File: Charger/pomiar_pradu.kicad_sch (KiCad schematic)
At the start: 13 parts, among them Q17 IRF7404, Q18 IRF7404, Q19 BC846, U10 MCP6001, U12 ACS712xLCTR-20A, U7 ACS712xLCTR-20A

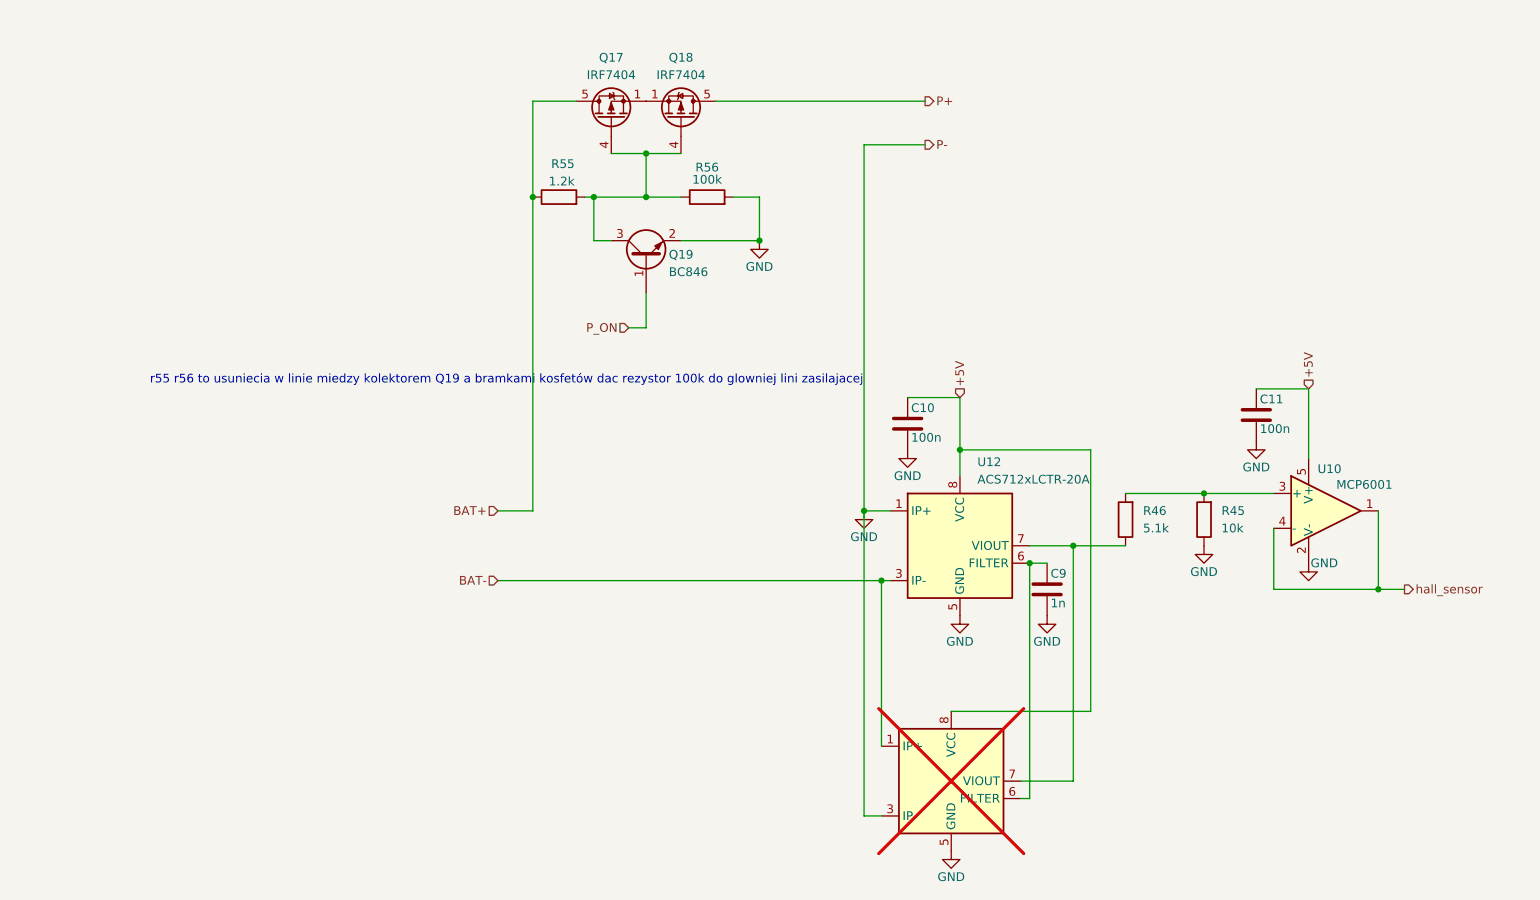
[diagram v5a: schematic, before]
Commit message: aktualizacja schematu
nie zmieniałem nic na pcb
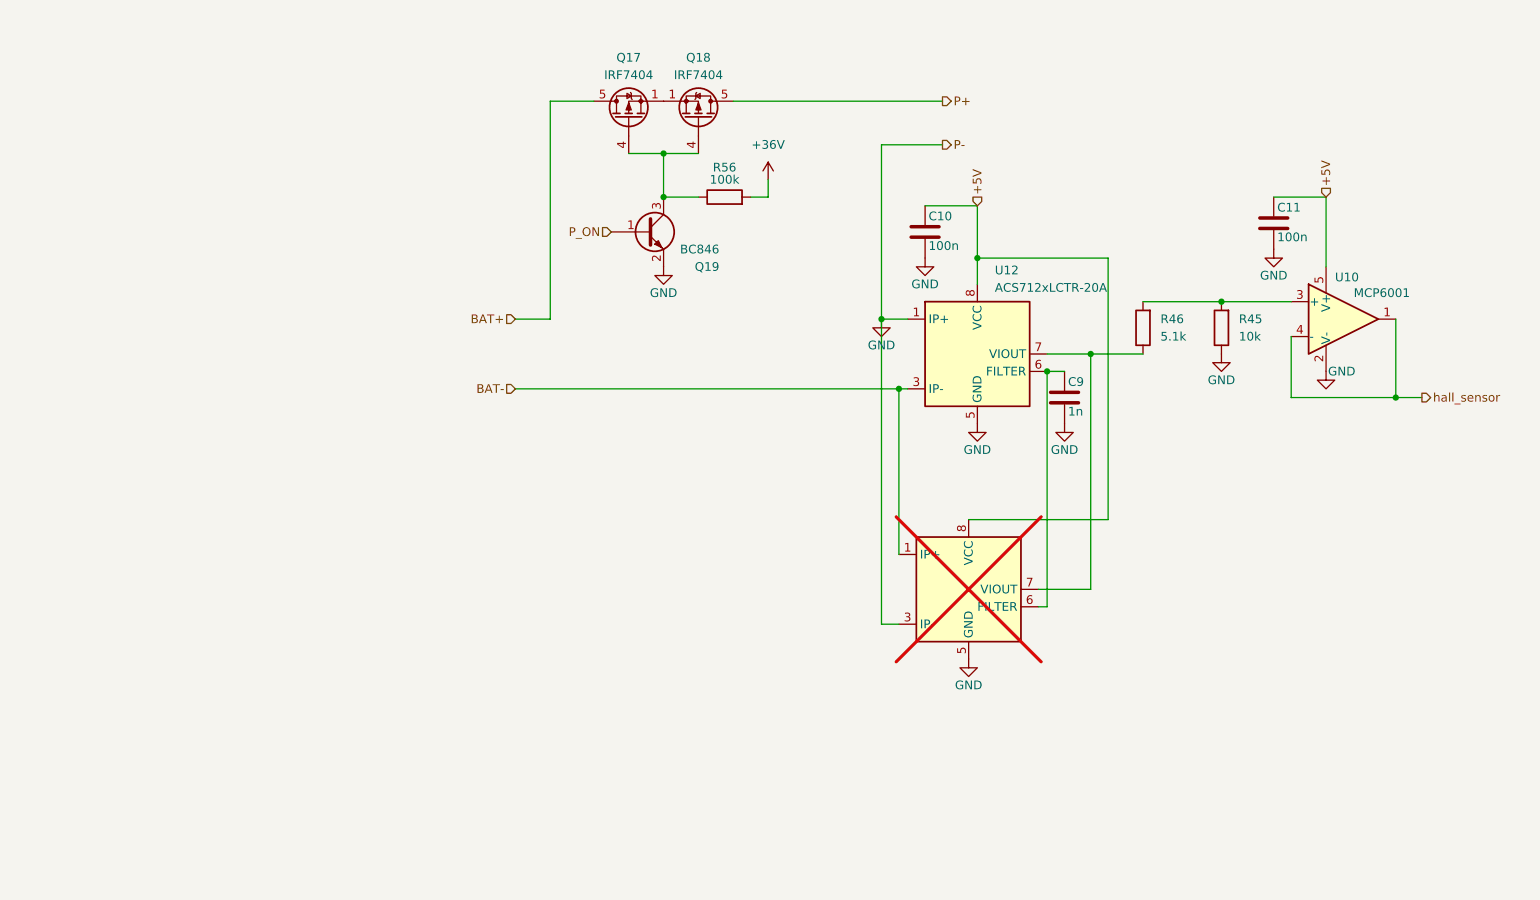
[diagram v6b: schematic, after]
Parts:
- removed R55: 1.2k, Resistor_SMD:R_0805_2012Metric_Pad1.20x1.40mm_HandSolder, symbol Device:R
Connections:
- net GND: no longer R56.2
- new net +36V: R56.2
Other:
- note removed: "r55 r56 to usuniecia w linie miedzy kolektorem Q19 a bramkami kosfetów dac rezystor 100k do glowniej lini zasilajacej"
- moved on the sheet: C10, C11, C9, Q17, Q18, Q19, R45, R46, R56, U10, U12
